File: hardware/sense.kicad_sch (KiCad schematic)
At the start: 10 parts, among them U10 AS5048A

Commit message: swd interface
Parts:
- R18: renamed from R?; value (none) -> 2Meg
- R19: renamed from R?; value (none) -> ~
- U11: renamed from U?; value (none) -> ~
- gave numbers to parts that had none: 2
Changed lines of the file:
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@@
   (symbol (lib_id "Device:R_US") (at 104.14 38.1 90) (unit 1)
     (in_bom yes) (on_board yes) (fields_autoplaced)
-    (property "Reference" "R?" (id 0) (at 104.14 31.75 90))
-    (property "Value" "" (id 1) (at 104.14 34.29 90))
+    (property "Reference" "R18" (id 0) (at 104.14 31.75 90))
+    (property "Value" "2Meg" (id 1) (at 104.14 34.29 90))
     (property "Footprint" "Resistor_SMD:R_0805_2012Metric" (id 2) (at 104.394 37.084 90)
       (effects (font (size 1.27 1.27)) hide)
@@
   (symbol (lib_id "power:GND") (at 88.9 45.72 0) (unit 1)
     (in_bom yes) (on_board yes) (fields_autoplaced)
-    (property "Reference" "#PWR?" (id 0) (at 88.9 52.07 0)
+    (property "Reference" "#PWR047" (id 0) (at 88.9 52.07 0)
       (effects (font (size 1.27 1.27)) hide)
     )
@@
   (symbol (lib_id "Device:Opamp_Dual") (at 135.89 40.64 0) (unit 1)
     (in_bom yes) (on_board yes) (fields_autoplaced)
-    (property "Reference" "U?" (id 0) (at 135.89 30.48 0))
-    (property "Value" "" (id 1) (at 135.89 33.02 0))
+    (property "Reference" "U11" (id 0) (at 135.89 30.48 0))
+    (property "Value" "~" (id 1) (at 135.89 33.02 0))
     (property "Footprint" "" (id 2) (at 135.89 40.64 0)
       (effects (font (size 1.27 1.27)) hide)
@@
   (symbol (lib_id "power:+12V") (at 222.25 29.21 0) (unit 1)
     (in_bom yes) (on_board yes) (fields_autoplaced)
-    (property "Reference" "#PWR?" (id 0) (at 222.25 33.02 0)
-      (effects (font (size 1.27 1.27)) hide)
-    )
-    (property "Value" "" (id 1) (at 222.25 24.13 0))
+    (property "Reference" "#PWR050" (id 0) (at 222.25 33.02 0)
+      (effects (font (size 1.27 1.27)) hide)
+    )
+    (property "Value" "~" (id 1) (at 222.25 24.13 0))
     (property "Footprint" "" (id 2) (at 222.25 29.21 0)
       (effects (font (size 1.27 1.27)) hide)
@@
   (symbol (lib_id "power:GND") (at 222.25 50.8 0) (unit 1)
     (in_bom yes) (on_board yes) (fields_autoplaced)
-    (property "Reference" "#PWR?" (id 0) (at 222.25 57.15 0)
+    (property "Reference" "#PWR051" (id 0) (at 222.25 57.15 0)
       (effects (font (size 1.27 1.27)) hide)
     )
@@
   (symbol (lib_id "Device:Opamp_Dual") (at 224.79 39.37 0) (unit 3)
     (in_bom yes) (on_board yes) (fields_autoplaced)
-    (property "Reference" "U?" (id 0) (at 223.52 38.0999 0)
-      (effects (font (size 1.27 1.27)) (justify left))
-    )
-    (property "Value" "" (id 1) (at 223.52 40.6399 0)
+    (property "Reference" "U11" (id 0) (at 223.52 38.0999 0)
+      (effects (font (size 1.27 1.27)) (justify left))
+    )
+    (property "Value" "~" (id 1) (at 223.52 40.6399 0)
       (effects (font (size 1.27 1.27)) (justify left))
     )
@@
   (symbol (lib_id "Device:R_US") (at 95.25 43.18 90) (unit 1)
     (in_bom yes) (on_board yes)
-    (property "Reference" "R?" (id 0) (at 95.25 38.1 90))
+    (property "Reference" "R17" (id 0) (at 95.25 38.1 90))
     (property "Value" "2Meg" (id 1) (at 95.25 40.64 90))
     (property "Footprint" "Resistor_SMD:R_0805_2012Metric" (id 2) (at 95.504 42.164 90)
@@
   (symbol (lib_id "power:GND") (at 93.98 73.66 0) (unit 1)
     (in_bom yes) (on_board yes) (fields_autoplaced)
-    (property "Reference" "#PWR047" (id 0) (at 93.98 80.01 0)
+    (property "Reference" "#PWR048" (id 0) (at 93.98 80.01 0)
       (effects (font (size 1.27 1.27)) hide)
     )
@@
   (symbol (lib_id "power:VAA") (at 111.76 22.86 0) (unit 1)
     (in_bom yes) (on_board yes) (fields_autoplaced)
-    (property "Reference" "#PWR?" (id 0) (at 111.76 26.67 0)
+    (property "Reference" "#PWR049" (id 0) (at 111.76 26.67 0)
       (effects (font (size 1.27 1.27)) hide)
     )
@@
   (symbol (lib_id "Device:R_Small_US") (at 135.89 50.8 90) (unit 1)
     (in_bom yes) (on_board yes) (fields_autoplaced)
-    (property "Reference" "R?" (id 0) (at 135.89 44.45 90))
+    (property "Reference" "R20" (id 0) (at 135.89 44.45 90))
     (property "Value" "10k" (id 1) (at 135.89 46.99 90))
     (property "Footprint" "Resistor_SMD:R_0805_2012Metric" (id 2) (at 135.89 50.8 0)
@@
   (symbol (lib_id "Device:Opamp_Dual") (at 198.12 29.21 0) (unit 2)
     (in_bom yes) (on_board yes) (fields_autoplaced)
-    (property "Reference" "U?" (id 0) (at 198.12 19.05 0))
-    (property "Value" "" (id 1) (at 198.12 21.59 0))
+    (property "Reference" "U11" (id 0) (at 198.12 19.05 0))
+    (property "Value" "~" (id 1) (at 198.12 21.59 0))
     (property "Footprint" "" (id 2) (at 198.12 29.21 0)
       (effects (font (size 1.27 1.27)) hide)
@@
   (symbol (lib_id "Device:R_US") (at 111.76 30.48 0) (mirror x) (unit 1)
     (in_bom yes) (on_board yes)
-    (property "Reference" "R?" (id 0) (at 116.84 30.48 90))
-    (property "Value" "" (id 1) (at 114.3 30.48 90))
+    (property "Reference" "R19" (id 0) (at 116.84 30.48 90))
+    (property "Value" "~" (id 1) (at 114.3 30.48 90))
     (property "Footprint" "Resistor_SMD:R_0805_2012Metric" (id 2) (at 112.776 30.226 90)
       (effects (font (size 1.27 1.27)) hide)

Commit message: led and other misc
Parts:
- R19: value ~ -> (none)
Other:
- moved on the sheet: R17
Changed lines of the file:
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@@
   (junction (at 81.28 66.04) (diameter 0) (color 0 0 0 0)
   )
-  (junction (at 148.59 40.64) (diameter 0) (color 0 0 0 0)
-  )
   (junction (at 76.2 76.2) (diameter 0) (color 0 0 0 0)
+  )
+  (junction (at 138.43 50.8) (diameter 0) (color 0 0 0 0)
+  )
+  (junction (at 146.05 40.64) (diameter 0) (color 0 0 0 0)
   )
   (junction (at 111.76 38.1) (diameter 0) (color 0 0 0 0)
@@
     (stroke (width 0) (type default) (color 0 0 0 0))
   )
-  (wire (pts (xy 148.59 40.64) (xy 148.59 50.8))
+  (wire (pts (xy 146.05 40.64) (xy 146.05 50.8))
     (stroke (width 0) (type default) (color 0 0 0 0))
   )
@@
     (stroke (width 0) (type default) (color 0 0 0 0))
   )
-  (wire (pts (xy 88.9 43.18) (xy 88.9 45.72))
-    (stroke (width 0) (type default) (color 0 0 0 0))
-  )
-  (wire (pts (xy 99.06 43.18) (xy 127 43.18))
+  (wire (pts (xy 101.6 43.18) (xy 101.6 45.72))
+    (stroke (width 0) (type default) (color 0 0 0 0))
+  )
+  (wire (pts (xy 121.92 43.18) (xy 127 43.18))
     (stroke (width 0) (type default) (color 0 0 0 0))
   )
@@
     (stroke (width 0) (type default) (color 0 0 0 0))
   )
-  (wire (pts (xy 148.59 40.64) (xy 163.83 40.64))
+  (wire (pts (xy 146.05 40.64) (xy 163.83 40.64))
     (stroke (width 0) (type default) (color 0 0 0 0))
   )
@@
     (stroke (width 0) (type default) (color 0 0 0 0))
   )
-  (wire (pts (xy 148.59 50.8) (xy 138.43 50.8))
+  (wire (pts (xy 146.05 50.8) (xy 138.43 50.8))
     (stroke (width 0) (type default) (color 0 0 0 0))
   )
@@
     (stroke (width 0) (type default) (color 0 0 0 0))
   )
-  (wire (pts (xy 143.51 40.64) (xy 148.59 40.64))
+  (wire (pts (xy 143.51 40.64) (xy 146.05 40.64))
+    (stroke (width 0) (type default) (color 0 0 0 0))
+  )
+  (wire (pts (xy 138.43 50.8) (xy 135.89 50.8))
     (stroke (width 0) (type default) (color 0 0 0 0))
   )
@@
     (stroke (width 0) (type default) (color 0 0 0 0))
   )
-  (wire (pts (xy 91.44 43.18) (xy 88.9 43.18))
+  (wire (pts (xy 114.3 43.18) (xy 101.6 43.18))
     (stroke (width 0) (type default) (color 0 0 0 0))
   )
@@
     (pin "2")
   )
-  (symbol (lib_id "power:GND") (at 88.9 45.72 0) (unit 1)
-    (in_bom yes) (on_board yes) (fields_autoplaced)
-    (property "Reference" "#PWR047" (id 0) (at 88.9 52.07 0)
-      (effects (font (size 1.27 1.27)) hide)
-    )
-    (property "Value" "GND" (id 1) (at 88.9 50.8 0))
-    (property "Footprint" "" (id 2) (at 88.9 45.72 0)
-      (effects (font (size 1.27 1.27)) hide)
-    )
-    (property "Datasheet" "" (id 3) (at 88.9 45.72 0)
+  (symbol (lib_id "power:+12V") (at 222.25 29.21 0) (unit 1)
+    (in_bom yes) (on_board yes) (fields_autoplaced)
+    (property "Reference" "#PWR?" (id 0) (at 222.25 33.02 0)
+      (effects (font (size 1.27 1.27)) hide)
+    )
+    (property "Value" "+12V" (id 1) (at 222.25 24.13 0))
+    (property "Footprint" "" (id 2) (at 222.25 29.21 0)
+      (effects (font (size 1.27 1.27)) hide)
+    )
+    (property "Datasheet" "" (id 3) (at 222.25 29.21 0)
+      (effects (font (size 1.27 1.27)) hide)
+    )
+    (pin "1")
+  )
+  (symbol (lib_id "power:GND") (at 101.6 45.72 0) (unit 1)
+    (in_bom yes) (on_board yes) (fields_autoplaced)
+    (property "Reference" "#PWR047" (id 0) (at 101.6 52.07 0)
+      (effects (font (size 1.27 1.27)) hide)
+    )
+    (property "Value" "GND" (id 1) (at 101.6 50.8 0))
+    (property "Footprint" "" (id 2) (at 101.6 45.72 0)
+      (effects (font (size 1.27 1.27)) hide)
+    )
+    (property "Datasheet" "" (id 3) (at 101.6 45.72 0)
       (effects (font (size 1.27 1.27)) hide)
     )
@@
     (pin "8")
   )
-  (symbol (lib_id "power:+12V") (at 222.25 29.21 0) (unit 1)
-    (in_bom yes) (on_board yes) (fields_autoplaced)
-    (property "Reference" "#PWR050" (id 0) (at 222.25 33.02 0)
-      (effects (font (size 1.27 1.27)) hide)
-    )
-    (property "Value" "~" (id 1) (at 222.25 24.13 0))
-    (property "Footprint" "" (id 2) (at 222.25 29.21 0)
-      (effects (font (size 1.27 1.27)) hide)
-    )
-    (property "Datasheet" "" (id 3) (at 222.25 29.21 0)
-      (effects (font (size 1.27 1.27)) hide)
-    )
-    (pin "1")
-  )
   (symbol (lib_id "power:GND") (at 222.25 50.8 0) (unit 1)
     (in_bom yes) (on_board yes) (fields_autoplaced)
@@
     (pin "8")
   )
-  (symbol (lib_id "Device:R_US") (at 95.25 43.18 90) (unit 1)
+  (symbol (lib_id "Device:R_US") (at 118.11 43.18 90) (unit 1)
     (in_bom yes) (on_board yes)
-    (property "Reference" "R17" (id 0) (at 95.25 38.1 90))
-    (property "Value" "2Meg" (id 1) (at 95.25 40.64 90))
-    (property "Footprint" "Resistor_SMD:R_0805_2012Metric" (id 2) (at 95.504 42.164 90)
-      (effects (font (size 1.27 1.27)) hide)
-    )
-    (property "Datasheet" "~" (id 3) (at 95.25 43.18 0)
-      (effects (font (size 1.27 1.27)) hide)
-    )
-    (property "Mouser" "https://www.mouser.com/ProductDetail/Panasonic/ERJ-6ENF5101V?qs=sGAEpiMZZMvdGkrng054t8AJgcdMkx7xVxAUQLZTFHA%3D" (id 4) (at 95.25 43.18 90)
+    (property "Reference" "R17" (id 0) (at 118.11 38.1 90))
+    (property "Value" "2Meg" (id 1) (at 118.11 40.64 90))
+    (property "Footprint" "Resistor_SMD:R_0805_2012Metric" (id 2) (at 118.364 42.164 90)
+      (effects (font (size 1.27 1.27)) hide)
+    )
+    (property "Datasheet" "~" (id 3) (at 118.11 43.18 0)
+      (effects (font (size 1.27 1.27)) hide)
+    )
+    (property "Mouser" "https://www.mouser.com/ProductDetail/Panasonic/ERJ-6ENF5101V?qs=sGAEpiMZZMvdGkrng054t8AJgcdMkx7xVxAUQLZTFHA%3D" (id 4) (at 118.11 43.18 90)
       (effects (font (size 1.27 1.27)) hide)
     )
@@
     (in_bom yes) (on_board yes)
     (property "Reference" "R19" (id 0) (at 116.84 30.48 90))
-    (property "Value" "~" (id 1) (at 114.3 30.48 90))
+    (property "Value" "" (id 1) (at 114.3 30.48 90))
     (property "Footprint" "Resistor_SMD:R_0805_2012Metric" (id 2) (at 112.776 30.226 90)
       (effects (font (size 1.27 1.27)) hide)

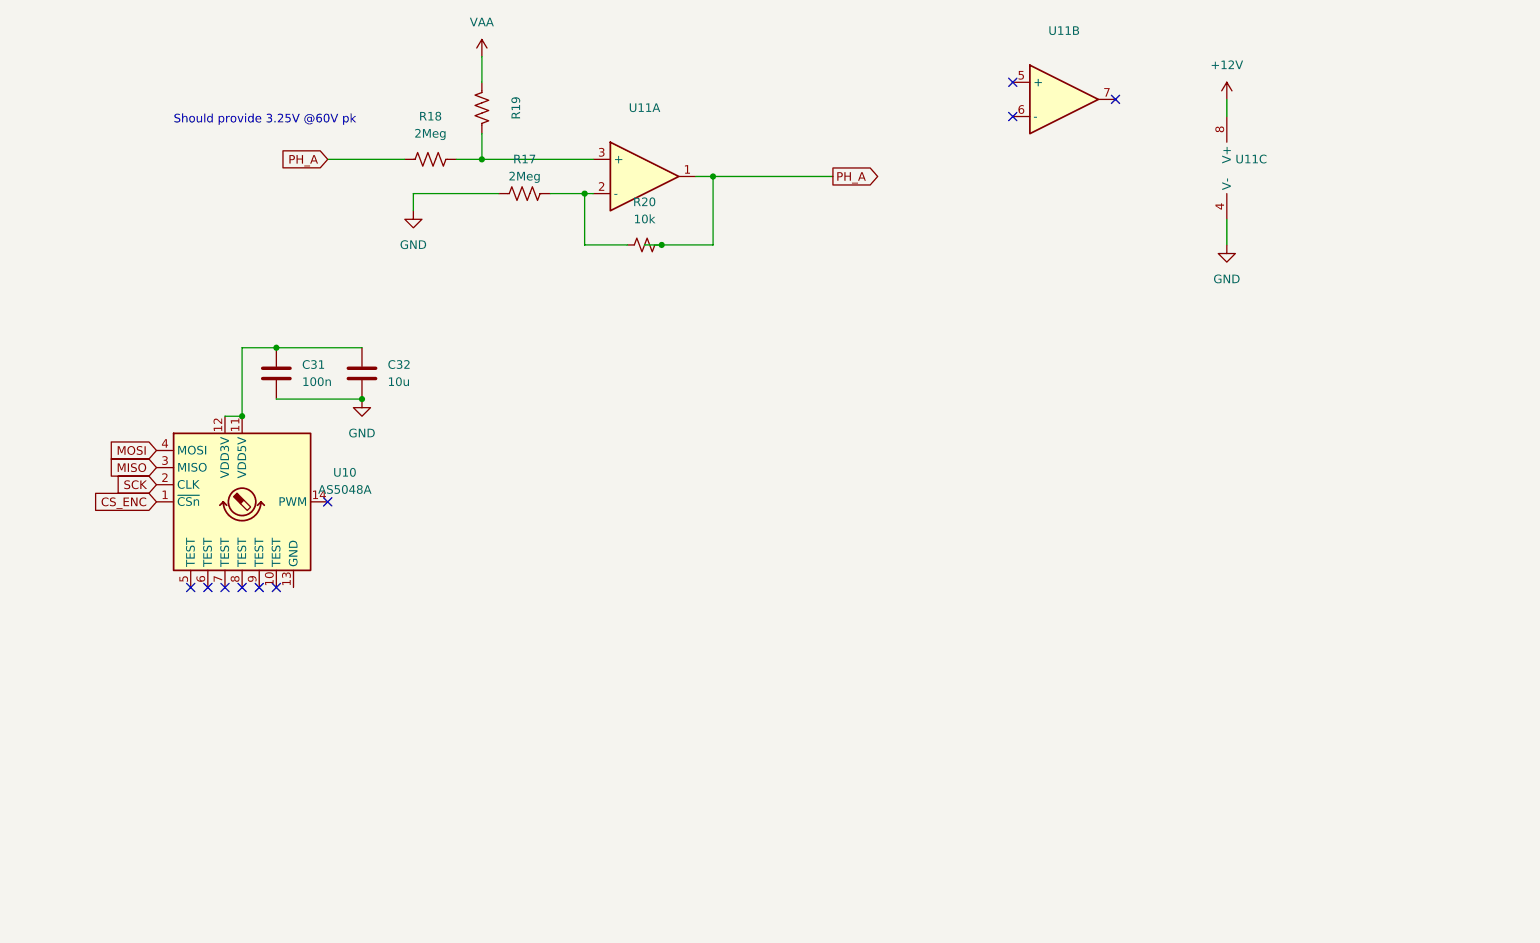
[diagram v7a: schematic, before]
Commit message: signal leds, bulk capacitance
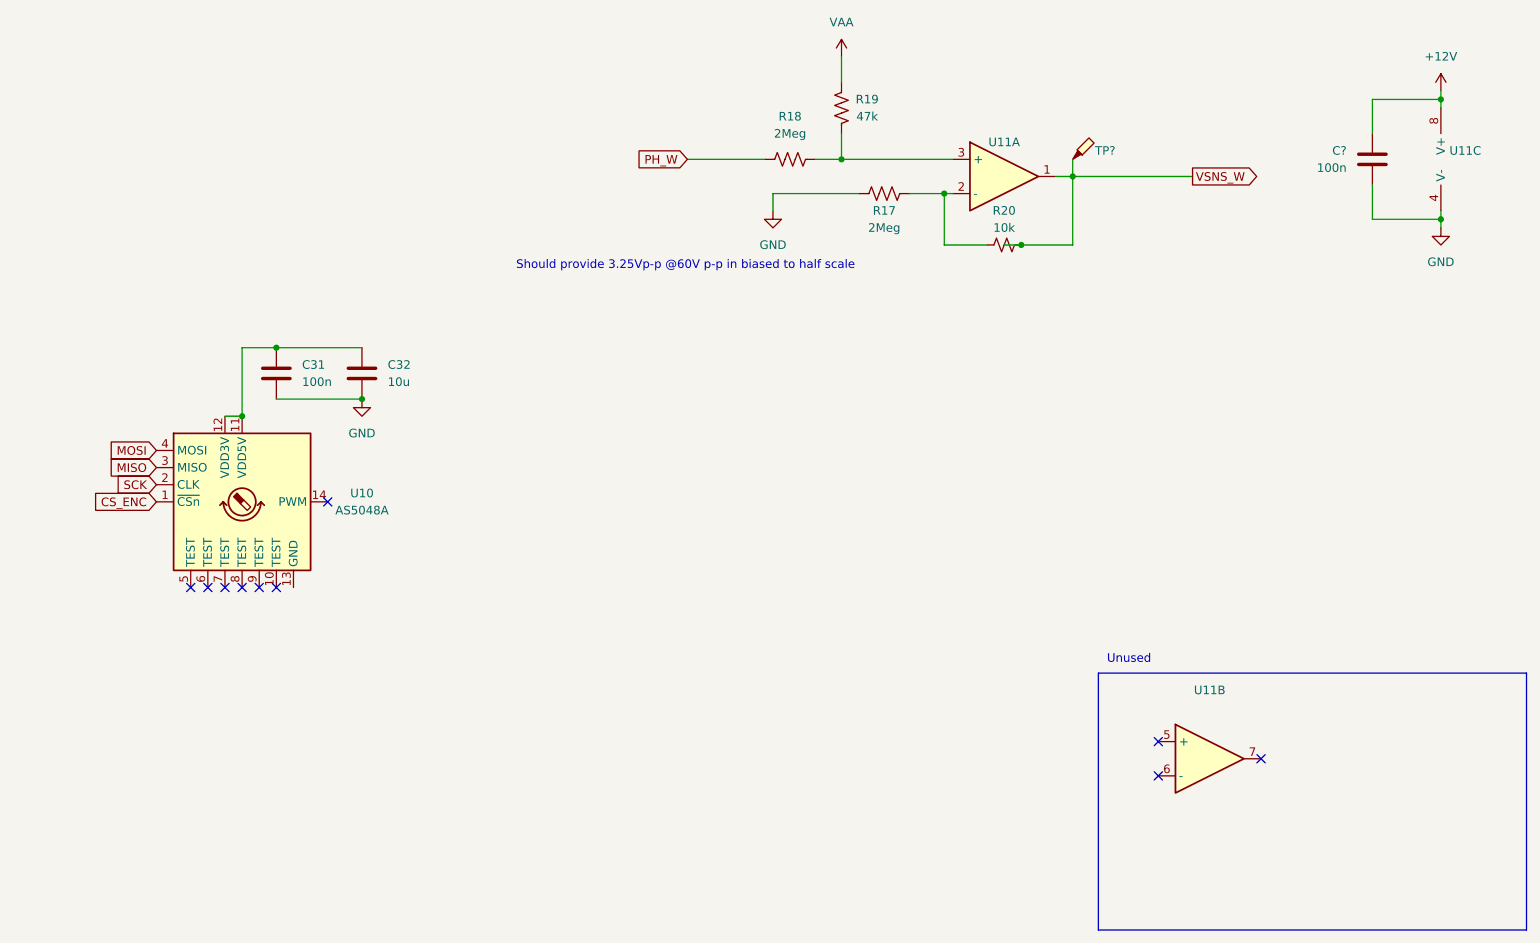
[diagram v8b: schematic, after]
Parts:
- added C?: 100n, Capacitor_SMD:C_0402_1005Metric, symbol Device:C
- added TP?: TestPoint_Probe, symbol Connector:TestPoint_Probe
- R19: value (none) -> 47k
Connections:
- net +12V: now also C?.2
- net GND: now also C?.1
- net PH_A renamed VSNS_W
- net VSNS_W: now also TP?.1; no longer R18.1
- new net PH_W: R18.1
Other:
- note added: "Should provide 3.25Vp-p @60V p-p in biased to half scale"
- note added: "Unused"
- note removed: "Should provide 3.25V @60V pk"
- moved on the sheet: R17, R18, R19, R20, U11A, U11B, U11C
